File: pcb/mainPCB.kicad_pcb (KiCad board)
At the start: 4 copper layers, 147.3 x 73 mm, 74 parts, among them J1 Inputs, J10 Conn_01x02_Male, J11 Conn_01x04_Male, J12 Conn_01x04_Male, J13 Conn_01x04_Male, J2 ESP32_left, J3 ESP32_right, J4 F9P_left_top, J5 F9P left bottom, J6 F9P right, J7 Motor A, J8 Motor B, J9 Power, K1 G5LE-1, U1 MMA8452Q, U2 AZ1117-5.0, U3 AZ1117-3.3, U4 AZ1117-5.0, U5 VNH7070AS, U6 VNH7070AS, U7 ADS1115IDGS, U8 PCA9306DCTR

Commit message: first version of the new feature set
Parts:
- removed J2: ESP32_left, Connector_PinSocket_2.54mm:PinSocket_1x15_P2.54mm_Vertical
- removed J6: F9P right, Connector_PinSocket_2.54mm:PinSocket_1x08_P2.54mm_Vertical
- added C23: 100p, Capacitor_SMD:C_0805_2012Metric, F.Cu at (133.8, 82.1)
- added C24: 1n, Capacitor_SMD:C_0805_2012Metric, F.Cu at (130.4, 74.1)
- added C25: 22u, Capacitor_SMD:C_0805_2012Metric, F.Cu at (130.2, 51.6)
- added C26: 100n, Capacitor_SMD:C_0805_2012Metric, F.Cu at (128.1, 51.6)
- added C27: 100n, Capacitor_SMD:C_0805_2012Metric, F.Cu at (118.2, 52.4)
- added C28: 100n, Capacitor_SMD:C_0805_2012Metric, F.Cu at (170.1, 55.4)
- added C29: 100n, Capacitor_SMD:C_0805_2012Metric, F.Cu at (159.8, 60.4)
- added C30: 100n, Capacitor_SMD:C_0805_2012Metric, F.Cu at (159.8, 62.5)
- added C31: 2.2u, Capacitor_SMD:C_0805_2012Metric, F.Cu at (159.8, 64.6)
- added C32: 100n, Capacitor_SMD:C_0805_2012Metric, F.Cu at (33.9, 90.6)
- added C33: 560u, Capacitor_SMD:CP_Elec_10x10.5, F.Cu at (44.1, 87.5)
- added C34: 1n/2000V, Capacitor_SMD:C_1206_3216Metric, F.Cu at (91.7, 51.7)
- added C35: 100n/16V, Capacitor_SMD:C_0805_2012Metric, F.Cu at (114.0, 54.0)
- added C36: 100n, Capacitor_SMD:C_0805_2012Metric, F.Cu at (97.8, 68.7)
- added C37: 22u, Capacitor_SMD:C_0805_2012Metric, F.Cu at (109.6, 67.3)
- added C38: 100n, Capacitor_SMD:C_0805_2012Metric, F.Cu at (109.6, 69.5)
- added C39: 100n, Capacitor_SMD:C_0805_2012Metric, F.Cu at (97.9, 72.1)
- added C40: 2.2u, Capacitor_SMD:C_0805_2012Metric, F.Cu at (97.9, 74.3)
- added C41: 100n, Capacitor_SMD:C_0805_2012Metric, F.Cu at (103.6, 74.6)
- added C42: 100n, Capacitor_SMD:C_0805_2012Metric, F.Cu at (151.1, 92.4)
- added C43: 100n, Capacitor_SMD:C_0805_2012Metric, F.Cu at (153.4, 89.5)
- added C44: 100n, Capacitor_SMD:C_0805_2012Metric, F.Cu at (156.9, 89.5)
- added C45: 100n, Capacitor_SMD:C_0805_2012Metric, F.Cu at (159.4, 92.4)
- added C46: 100n, Capacitor_SMD:C_0805_2012Metric, F.Cu at (156.4, 100.3)
- added C47: 10n, Capacitor_SMD:C_0805_2012Metric, F.Cu at (175.4, 94.4)
- added C48: 100n, Capacitor_SMD:C_0805_2012Metric, F.Cu at (173.2, 94.4)
- added C49: 100n, Capacitor_SMD:C_0805_2012Metric, F.Cu at (169.4, 97.7)
- added C50: 10u, Capacitor_SMD:C_0805_2012Metric, F.Cu at (169.4, 93.4)
- added C51: 100n, Capacitor_SMD:C_0805_2012Metric, F.Cu at (169.4, 95.6)
- added D10: BAT54C, Package_TO_SOT_SMD:SOT-23, F.Cu at (149.2, 79.0)
- added D11: SD0805S020S1R0, Diode_SMD:D_0805_2012Metric, F.Cu at (161.2, 54.4)
- added D4: LED/red, Capacitor_SMD:C_0805_2012Metric, F.Cu at (75.8, 106.7)
- added D5: LED/red, Capacitor_SMD:C_0805_2012Metric, F.Cu at (63.8, 48.5)
- added D6: LED/red, Capacitor_SMD:C_0805_2012Metric, F.Cu at (68.1, 48.5)
- added D7: SD0805S020S1R0, Diode_SMD:D_0805_2012Metric, F.Cu at (67.6, 55.4)
- added D8: SD0805S020S1R0, Diode_SMD:D_0805_2012Metric, F.Cu at (53.8, 94.7)
- added D9: LED/green, Capacitor_SMD:C_0805_2012Metric, F.Cu at (79.2, 106.8)
- added F1: 12A/slow, ICs_own:Fuse_1206_3216Metric, F.Cu at (53.1, 53.2)
- added FB1: 600R/2A, Inductor_SMD:L_0805_2012Metric, F.Cu at (109.6, 71.6)
- added H6: MountingHole, MountingHole:MountingHole_3.2mm_M3_DIN965, F.Cu at (28.6, 65.5)
- added H7: MountingHole, MountingHole:MountingHole_3.2mm_M3_DIN965, F.Cu at (28.6, 82.4)
- added H8: MountingHole, MountingHole:MountingHole_3.2mm_M3_DIN965, F.Cu at (115.2, 59.1)
- added IC1: FXL6408UMX, ICs_own:QFN40P180X260X55-16N, F.Cu at (73.5, 97.9)
- added IC2: ATA6561-GAQW-N, ICs_own:SOIC127P600X175-8N, F.Cu at (123.1, 51.5)
- added IC3: ICL3221EIVZ, ICs_own:SOP65P640X120-16N, F.Cu at (155.3, 95.1)
- added J14: USB_B_Micro, Connector_own:USB_Micro-B_Molex-105017-0001, F.Cu at (174.6, 52.8)
- added J15: RJ45_Amphenol_RJMG1BD3B8K1ANR, Connector_own:RJ45_Amphenol_RJMG1BD3B8K1ANR, F.Cu at (106.9, 54.9)
- added J16: DB9_Male_MountingHoles, Connector_own:LD09P33E4GV00LF, F.Cu at (179.4, 74.0)
- added J17: SM04B-SRSS-TB(LF)(SN), Connector_own:JST_SH_SM04B-SRSS-TB_1x04-1MP_P1.00mm_Horizontal, F.Cu at (156.5, 106.9)
- added J18: PTSM-Header-Horizontal-2, Connector_own:1814841, F.Cu at (116.8, 44.7)
- added K2: CP1SA-12V-Z, Relay_own:CP1SA12VZ, F.Cu at (82.0, 61.6)
- added L1: 22u, Inductor_SMD:L_0805_2012Metric, F.Cu at (132.8, 51.6)
- added PS1: V78E05-1000-SMT-TR, ICs_own:SOP254P1140X825-10N, F.Cu at (59.9, 86.6)
- added Q1: BC817-40,215, ICs_own:SOT95P230X110-3N, F.Cu at (154.4, 71.1)
- added Q2: BC817-40,215, ICs_own:SOT95P230X110-3N, F.Cu at (149.0, 71.1)
- added R23: 2.4k, Resistor_SMD:R_0805_2012Metric, F.Cu at (157.2, 49.8)
- added R24: 2.4k, Resistor_SMD:R_0805_2012Metric, F.Cu at (162.7, 49.8)
- added R25: 240, Resistor_SMD:R_0805_2012Metric, F.Cu at (139.8, 51.6)
- added R26: 2.4k, Resistor_SMD:R_0805_2012Metric, F.Cu at (139.0, 92.5)
- added R27: 2.4k, Resistor_SMD:R_0805_2012Metric, F.Cu at (139.1, 90.2)
- added R28: 220k, Resistor_SMD:R_0805_2012Metric, F.Cu at (133.7, 79.8)
- added R29: 2.4k, Resistor_SMD:R_0805_2012Metric, F.Cu at (122.7, 90.2)
- added R30: 2.4k, Resistor_SMD:R_0805_2012Metric, F.Cu at (122.7, 92.2)
- added R31: 2.4k, Resistor_SMD:R_0805_2012Metric, F.Cu at (130.5, 69.7)
- added R32: 620, Resistor_SMD:R_0805_2012Metric, F.Cu at (130.5, 71.9)
- added R33: 120, Resistor_SMD:R_0805_2012Metric, F.Cu at (119.6, 55.8)
- added R34: 22.1k, Resistor_SMD:R_0805_2012Metric, F.Cu at (165.9, 55.4)
- added R35: 47k, Resistor_SMD:R_0805_2012Metric, F.Cu at (165.9, 53.2)
- added R36: 1k, Resistor_SMD:R_0805_2012Metric, F.Cu at (160.5, 57.3)
- added R37: 1k, Resistor_SMD:R_0805_2012Metric, F.Cu at (151.8, 64.5)
- added R38: 120, Resistor_SMD:R_0805_2012Metric, F.Cu at (143.3, 58.0)
- added R39: 120, Resistor_SMD:R_0805_2012Metric, F.Cu at (141.0, 58.0)
- added R40: 1k, Resistor_SMD:R_0805_2012Metric, F.Cu at (151.8, 66.9)
- added R41: 120, Resistor_SMD:R_0805_2012Metric, F.Cu at (153.6, 79.0)
- added R42: 0, Resistor_SMD:R_0805_2012Metric, F.Cu at (91.7, 56.2)
- added R43: 2.4k, Resistor_SMD:R_0805_2012Metric, F.Cu at (91.7, 46.8)
- added R44: 0, Resistor_SMD:R_0805_2012Metric, F.Cu at (113.9, 50.8)
- added R45: 49.9, Resistor_SMD:R_0805_2012Metric, F.Cu at (107.9, 61.7)
- added R46: 49.9, Resistor_SMD:R_0805_2012Metric, F.Cu at (97.8, 64.3)
- added R47: 49.9, Resistor_SMD:R_0805_2012Metric, F.Cu at (107.8, 65.0)
- added R48: 12.1k, Resistor_SMD:R_0805_2012Metric, F.Cu at (97.7, 66.4)
- added R49: 49.9, Resistor_SMD:R_0805_2012Metric, F.Cu at (97.7, 61.1)
- added R50: 2.4k, Resistor_SMD:R_0805_2012Metric, F.Cu at (113.9, 47.5)
- added R51: 2.4k, Resistor_SMD:R_0805_2012Metric, F.Cu at (111.0, 76.6)
- added R52: 2.4k, Resistor_SMD:R_0805_2012Metric, F.Cu at (111.0, 78.9)
- added R53: 2.4k, Resistor_SMD:R_0805_2012Metric, F.Cu at (111.0, 74.5)
- added R54: 24, Resistor_SMD:R_0805_2012Metric, F.Cu at (169.4, 91.3)
- added SW1: SW_Push, Button_Switch_SMD:SW_SPST_PTS645, F.Cu at (127.0, 97.3)
- added U10: NUD3124LT1G, ICs_own:SOT95P237X100-3N, F.Cu at (72.3, 70.2)
- added U11: LAN8720A, Package_DFN_QFN:QFN-24-1EP_4x4mm_P0.5mm_EP2.6x2.6mm, F.Cu at (102.8, 70.7)
- added U12: LSM9DS1, Package_LGA:LGA-24L_3x3.5mm_P0.43mm, F.Cu at (174.3, 98.2)
- added U9: VNH7070AS, Package_SO:SOIC-16_3.9x9.9mm_P1.27mm, F.Cu at (28.4, 91.2)
- C1, C10, C21, C3, C9: footprint Capacitor_SMD:C_0805_2012Metric_Pad1.15x1.40mm_HandSolder -> Capacitor_SMD:C_0805_2012Metric
- C11: value 22n -> 22u; footprint Capacitor_SMD:C_0805_2012Metric_Pad1.15x1.40mm_HandSolder -> Capacitor_SMD:C_0805_2012Metric
- C12, C8: value 10u -> 100n; footprint Capacitor_SMD:C_0805_2012Metric_Pad1.15x1.40mm_HandSolder -> Capacitor_SMD:C_0805_2012Metric
- C13: value 100n -> 560u; footprint Capacitor_SMD:C_0805_2012Metric_Pad1.15x1.40mm_HandSolder -> Capacitor_SMD:CP_Elec_10x10.5
- C14: value 470u -> 1n; footprint Capacitor_THT:CP_Radial_D8.0mm_P3.80mm -> Capacitor_SMD:C_0805_2012Metric
- C15: value 100n -> 1n; footprint Capacitor_SMD:C_0805_2012Metric_Pad1.15x1.40mm_HandSolder -> Capacitor_SMD:C_0805_2012Metric
- C16: value 22u -> 100p; footprint Capacitor_SMD:C_0805_2012Metric_Pad1.15x1.40mm_HandSolder -> Capacitor_SMD:C_0805_2012Metric
- C17, C18: value 1n -> 100p; footprint Capacitor_SMD:C_0805_2012Metric_Pad1.15x1.40mm_HandSolder -> Capacitor_SMD:C_0805_2012Metric
- C19: value 100p -> 100n; footprint Capacitor_SMD:C_0805_2012Metric_Pad1.15x1.40mm_HandSolder -> Capacitor_SMD:C_0805_2012Metric
- C2: value 4.7u -> 100n; footprint Capacitor_SMD:C_0805_2012Metric_Pad1.15x1.40mm_HandSolder -> Capacitor_SMD:C_0805_2012Metric
- C20: value 100p -> 22u; footprint Capacitor_SMD:C_0805_2012Metric_Pad1.15x1.40mm_HandSolder -> Capacitor_SMD:C_0805_2012Metric
- C22: value 100p -> 560u; footprint Capacitor_SMD:C_0805_2012Metric_Pad1.15x1.40mm_HandSolder -> Capacitor_SMD:CP_Elec_10x10.5
- C4: value 22u -> 100n; footprint Capacitor_SMD:C_0805_2012Metric_Pad1.15x1.40mm_HandSolder -> Capacitor_SMD:C_0805_2012Metric
- C5: value 2200u -> 22u; footprint Capacitor_THT:CP_Radial_D14.0mm_P5.00mm -> Capacitor_SMD:C_0805_2012Metric
- C6: value 10u -> 560u; footprint Capacitor_SMD:C_0805_2012Metric_Pad1.15x1.40mm_HandSolder -> Capacitor_SMD:CP_Elec_10x10.5
- C7: value 22u -> 10u; footprint Capacitor_SMD:C_0805_2012Metric_Pad1.15x1.40mm_HandSolder -> Capacitor_SMD:C_0805_2012Metric
- D1: value Network -> LED/blue; footprint LED_SMD:LED_0805_2012Metric_Pad1.15x1.40mm_HandSolder -> Capacitor_SMD:C_0805_2012Metric
- D2: value NTRIP -> LED/blue; footprint LED_SMD:LED_0805_2012Metric_Pad1.15x1.40mm_HandSolder -> Capacitor_SMD:C_0805_2012Metric
- D3: value SD0805S020S1R0 -> LED/green; footprint Diode_SMD:D_0805_2012Metric_Pad1.15x1.40mm_HandSolder -> Capacitor_SMD:C_0805_2012Metric
- H5: footprint MountingHole:MountingHole_4.3mm_M4_DIN965 -> MountingHole:MountingHole_3.2mm_M3_DIN965
- J1: value Inputs -> PTSM-Header-Horizontal-6; footprint TerminalBlock_Phoenix:TerminalBlock_Phoenix_MPT-0,5-8-2.54_1x08_P2.54mm_Horizontal -> Connector_own:1814883
- J10: value Conn_01x02_Male -> Conn_01x08_Female; footprint Connector_PinHeader_2.54mm:PinHeader_1x02_P2.54mm_Vertical -> Connector_PinSocket_2.54mm:PinSocket_1x08_P2.54mm_Vertical
- J11: value Conn_01x04_Male -> Conn_01x08_Female; footprint Connector_PinHeader_2.54mm:PinHeader_1x04_P2.54mm_Vertical -> Connector_PinSocket_2.54mm:PinSocket_1x08_P2.54mm_Vertical
- J12: value Conn_01x04_Male -> Conn_02x02_Odd_Even; footprint Connector_PinHeader_2.54mm:PinHeader_1x04_P2.54mm_Vertical -> Connector_PinHeader_2.54mm:PinHeader_2x02_P2.54mm_Horizontal
- J13: value Conn_01x04_Male -> SM04B-SRSS-TB(LF)(SN); footprint Connector_PinHeader_2.54mm:PinHeader_1x04_P2.54mm_Vertical -> Connector_own:JST_SH_SM04B-SRSS-TB_1x04-1MP_P1.00mm_Horizontal
- J3: value ESP32_right -> PTSM-Header-Horizontal-7; footprint Connector_PinSocket_2.54mm:PinSocket_1x15_P2.54mm_Vertical -> Connector_own:1814896
- J4: value F9P_left_top -> CCA-Header-Horizontal-4; footprint Connector_PinSocket_2.54mm:PinSocket_1x08_P2.54mm_Vertical -> Connector_own:1836366
- J5: value F9P left bottom -> PTSM-Header-Horizontal-5; footprint Connector_PinSocket_2.54mm:PinSocket_1x08_P2.54mm_Vertical -> Connector_own:1814870
- J7: value Motor A -> Conn_01x04_Male; footprint TerminalBlock_Phoenix:TerminalBlock_Phoenix_MKDS-1,5-2-5.08_1x02_P5.08mm_Horizontal -> Connector_PinHeader_2.54mm:PinHeader_1x04_P2.54mm_Horizontal
- J8: value Motor B -> Conn_01x04_Male; footprint TerminalBlock_Phoenix:TerminalBlock_Phoenix_MKDS-1,5-2-5.08_1x02_P5.08mm_Horizontal -> Connector_PinHeader_2.54mm:PinHeader_1x04_P2.54mm_Vertical
- J9: value Power -> Conn_01x08_Female; footprint TerminalBlock_Phoenix:TerminalBlock_Phoenix_MKDS-1,5-2-5.08_1x02_P5.08mm_Horizontal -> Connector_PinSocket_2.54mm:PinSocket_1x08_P2.54mm_Vertical
- K1: value G5LE-1 -> CP1SA-12V-Z; footprint Relay_THT:Relay_SPDT_Omron-G5LE-1 -> Relay_own:CP1SA12VZ
- R1: value 47 -> 120; footprint Resistor_SMD:R_0805_2012Metric_Pad1.15x1.40mm_HandSolder -> Resistor_SMD:R_0805_2012Metric
- R10: value 1k -> 47k; footprint Resistor_SMD:R_0805_2012Metric_Pad1.15x1.40mm_HandSolder -> Resistor_SMD:R_0805_2012Metric
- R11, R12, R18, R20, R7, R8, R9: footprint Resistor_SMD:R_0805_2012Metric_Pad1.15x1.40mm_HandSolder -> Resistor_SMD:R_0805_2012Metric
- R13: value 2.4k -> 1k; footprint Resistor_SMD:R_0805_2012Metric_Pad1.15x1.40mm_HandSolder -> Resistor_SMD:R_0805_2012Metric
- R14: value 620 -> 2.4k; footprint Resistor_SMD:R_0805_2012Metric_Pad1.15x1.40mm_HandSolder -> Resistor_SMD:R_0805_2012Metric
- R15: value 2.4k -> 24; footprint Resistor_SMD:R_0805_2012Metric_Pad1.15x1.40mm_HandSolder -> Resistor_SMD:R_0805_2012Metric
- R16: value 620 -> 24; footprint Resistor_SMD:R_0805_2012Metric_Pad1.15x1.40mm_HandSolder -> Resistor_SMD:R_0805_2012Metric
- R17, R21: value 2.4k -> 620; footprint Resistor_SMD:R_0805_2012Metric_Pad1.15x1.40mm_HandSolder -> Resistor_SMD:R_0805_2012Metric
- R19: value 220k -> 620; footprint Resistor_SMD:R_0805_2012Metric_Pad1.15x1.40mm_HandSolder -> Resistor_SMD:R_0805_2012Metric
- R2, R3: value 160 -> 620; footprint Resistor_SMD:R_0805_2012Metric_Pad1.15x1.40mm_HandSolder -> Resistor_SMD:R_0805_2012Metric
- R22: value 24 -> 2.4k; footprint Resistor_SMD:R_0805_2012Metric_Pad1.15x1.40mm_HandSolder -> Resistor_SMD:R_0805_2012Metric
- R4, R5: value 4.7k -> 620; footprint Resistor_SMD:R_0805_2012Metric_Pad1.15x1.40mm_HandSolder -> Resistor_SMD:R_0805_2012Metric
- R6: value 24 -> 47k; footprint Resistor_SMD:R_0805_2012Metric_Pad1.15x1.40mm_HandSolder -> Resistor_SMD:R_0805_2012Metric
- U1: value MMA8452Q -> ESP32-WROOM-32; footprint Package_LGA:LGA-16_3x3mm_P0.5mm_LayoutBorder3x5y -> RF_Module:ESP32-WROOM-32
- U2: value AZ1117-5.0 -> AZ1117-3.3
- U3: value AZ1117-3.3 -> VNH7070AS; footprint Package_TO_SOT_SMD:SOT-223-3_TabPin2 -> Package_SO:SOIC-16_3.9x9.9mm_P1.27mm
- U4: value AZ1117-5.0 -> ADS1115IDGS; footprint Package_TO_SOT_SMD:SOT-223-3_TabPin2 -> Package_SO:MSOP-10_3x3mm_P0.5mm
- U6: value VNH7070AS -> PCA9306DCTR; footprint Package_SO:SOIC-16_3.9x9.9mm_P1.27mm -> Package_SO:SSOP-8_2.95x2.8mm_P0.65mm
- U7: value ADS1115IDGS -> TPD3E001DRLR; footprint Package_SO:MSOP-10_3x3mm_P0.5mm -> Package_TO_SOT_SMD:SOT-553
- U8: value PCA9306DCTR -> CP2102N-A01-GQFN24; footprint Package_SO:SSOP-8_2.95x2.8mm_P0.65mm -> Package_DFN_QFN:QFN-24-1EP_4x4mm_P0.5mm_EP2.6x2.6mm
- moved U5 237.4 mm to (28.4, 73.9), turned to 0 degrees
- moved C13 219.7 mm to (44.1, 59.2), turned to 270 degrees
- moved K1 216.7 mm to (58.9, 66.3), turned to 90 degrees
- moved C12 215.3 mm to (33.7, 55.8)
- moved D3 213.6 mm to (72.6, 106.7)
- moved R6 211.7 mm to (77.9, 97.2), turned to 270 degrees
- moved U3 190.7 mm to (28.3, 56.8), turned to 0 degrees
- moved R7 190.4 mm to (58.0, 108.5), turned to 0 degrees
- moved R12 190.2 mm to (58.0, 97.7), turned to 0 degrees
- moved R11 189.8 mm to (58.0, 99.8), turned to 0 degrees
- moved C8 189.4 mm to (59.1, 79.2), turned to 0 degrees
- moved R8 188.4 mm to (58.0, 106.3), turned to 0 degrees
- moved D2 188.3 mm to (69.3, 106.7), turned to 90 degrees
- moved R9 187.0 mm to (58.0, 104.1), turned to 0 degrees
- moved J8 185.0 mm to (76.5, 82.7)
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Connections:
- C1 pad 1: +3V3 -> GND
- C1 pad 2: GND -> Net-(C1-Pad2)
- C10 pad 1: Net-(C10-Pad1) -> +5V
- C11 pad 1: GND -> +3V3
- C11 pad 2: Net-(C11-Pad2) -> GND
- C14 pad 1: +12V -> /Input_1/output
- C15 pad 1: +12V -> /Input_2/output
- C16 pad 1: +5V -> Net-(C16-Pad1)
- C17 pad 1: /Workswitch/output -> Net-(C17-Pad1)
- C18 pad 1: /AutosteerSwitch/output -> Net-(C18-Pad1)
- C20 pad 1: Net-(C20-Pad1) -> Net-(C19-Pad1)
- C21 pad 1: +5V -> +12V
- C22 pad 1: Net-(C22-Pad1) -> +12V
- C3 pad 1: Net-(C3-Pad1) -> /ESP_EN
- C4 pad 1: GND -> +3V3
- C4 pad 2: +3V3 -> GND
- C5 pad 1: +12V -> +3V3
- C6 pad 1: +5V -> Net-(C6-Pad1)
- C7 pad 1: +3V3 -> Net-(C6-Pad1)
- C8 pad 1: +12V -> Net-(C8-Pad1)
- D3 pad 1: +12V -> GND
- J1 pad 1: /Workswitch/input -> Net-(C1-Pad2)
- J1 pad 2: Net-(C11-Pad2) -> /Input_1/input
- J1 pad 3: /AutosteerSwitch/input -> Net-(C1-Pad2)
- J1 pad 4: Net-(C11-Pad2) -> /Input_2/input
- J1 pad 5: Net-(J1-Pad5) -> Net-(C1-Pad2)
- J1 pad 6: /SteeringAngle/In_A -> /Input_3/input
- J10 pad 1: +5V -> /F9P/RX2
- J10 pad 2: /SteeringAngle/In_A -> Net-(J10-Pad2)
- J11 pad 1: /I2C_SDA -> Net-(J11-Pad1)
- J11 pad 2: /I2C_SCL -> GND
- J11 pad 4: +3V3 -> +5V
- J12 pad 1: +12V -> Net-(IC2-Pad1)
- J12 pad 2: +5V -> /CAN_TXD
- J12 pad 3: +3V3 -> Net-(IC2-Pad6)
- J12 pad 4: GND -> Net-(J12-Pad4)
- J13 pad 1: Net-(J13-Pad1) -> GND
- J13 pad 2: Net-(J13-Pad2) -> +3V3
- J13 pad 3: GND -> /I2C_3_SCL
- J13 pad 4: +5V -> /I2C_3_SDA
- J3 pad 1: /VSPI_MOSI -> /Relais/COM
- J3 pad 2: /I2C_SCL -> /Relais/NC
- J3 pad 3: Net-(J3-Pad3) -> /Relais/NO
- J3 pad 4: Net-(J3-Pad4) -> /sheet5C9DA53F/outB
- J3 pad 5: /I2C_SDA -> GND
- J3 pad 6: /VSPI_MISO -> /sheet5C9DA53F/outA
- J3 pad 7: /VSPI_CLK -> GND
- J4 pad 1: Net-(J4-Pad1) -> GND
- J4 pad 2: Net-(J4-Pad2) -> /powerSupply/V_In_12V
- J4 pad 3: Net-(J3-Pad9) -> /motorDriverA/outA
- J4 pad 4: Net-(J4-Pad4) -> /motorDriverA/outB
- J5 pad 1: Net-(J3-Pad10) -> Net-(J5-Pad1)
- J5 pad 3: Net-(J5-Pad3) -> GND
- J7 pad 1: /motorDriverA/outA -> +5V
- J7 pad 2: /motorDriverA/outB -> GND
- J8 pad 1: /motorDriverB/outA -> +3V3
- J8 pad 2: /motorDriverB/outB -> GND
- J9 pad 1: /powerSupply/V_In_12V -> /RXD01
- J9 pad 2: GND -> /TXD01
- K1 pad 2: +12V -> Net-(D5-Pad1)
- K1 pad 3: /powerSupply/V_In_12V -> +12V
- K1 pad 4: Net-(K1-Pad4) -> GND
- K1 pad 5: GND -> Net-(D6-Pad2)
- R1 pad 2: Net-(C11-Pad2) -> Net-(C1-Pad2)
- R10 pad 1: Net-(R10-Pad1) -> +3V3
- R10 pad 2: /motorDriverB/INA -> /ESP_EN
- R11 pad 1: Net-(R11-Pad1) -> /motorDriverA/INA
- R11 pad 2: /motorDriverB/InB -> /M1_INA
- R12 pad 1: Net-(R12-Pad1) -> /motorDriverA/InB
- R12 pad 2: /motorDriverB/PWM -> /M1_INB
- R13 pad 1: /Workswitch/output -> /motorDriverA/PWM
- R13 pad 2: /Workswitch/input -> /M1_PWM
- R14 pad 1: /Workswitch/output -> GND
- R14 pad 2: GND -> Net-(D5-Pad2)
- R15 pad 1: /AutosteerSwitch/output -> Net-(D7-Pad2)
- R15 pad 2: /AutosteerSwitch/input -> Net-(D5-Pad1)
- R16 pad 1: /AutosteerSwitch/output -> Net-(D7-Pad2)
- R16 pad 2: GND -> Net-(D5-Pad1)
- R17 pad 1: Net-(C19-Pad1) -> +3V3
- R17 pad 2: /SteeringAngle/IN_B -> Net-(D9-Pad2)
- R18 pad 1: Net-(C20-Pad1) -> /Input_1/output
- R18 pad 2: /SteeringAngle/In_A -> /Input_1/input
- R19 pad 1: +5V -> /Input_1/output
- R19 pad 2: Net-(C22-Pad1) -> GND
- R2 pad 1: Net-(J2-Pad6) -> Net-(D1-Pad2)
- R2 pad 2: Net-(D1-Pad2) -> Net-(IC1-Pad7)
- R20 pad 1: Net-(J13-Pad2) -> /Input_2/output
- R20 pad 2: +5V -> /Input_2/input
- R21 pad 1: Net-(J13-Pad1) -> /Input_2/output
- R21 pad 2: +5V -> GND
- R22 pad 1: Net-(D3-Pad2) -> Net-(C16-Pad1)
- R22 pad 2: /powerSupply/V_In_12V -> Net-(J5-Pad5)
- R3 pad 1: Net-(J2-Pad7) -> Net-(D2-Pad2)
- R3 pad 2: Net-(D2-Pad2) -> Net-(IC1-Pad8)
- R4 pad 1: +3V3 -> Net-(D3-Pad2)
- R4 pad 2: /I2C_SCL -> Net-(IC1-Pad11)
- R5 pad 1: +3V3 -> Net-(D4-Pad2)
- R5 pad 2: /I2C_SDA -> Net-(IC1-Pad12)
- R6 pad 1: Net-(D3-Pad2) -> +3V3
- R6 pad 2: /powerSupply/V_In_12V -> Net-(IC1-Pad10)
- R7 pad 1: Net-(R7-Pad1) -> /sheet5C9DA53F/INA
- R7 pad 2: /motorDriverA/INA -> /M2_INA
- R8 pad 1: Net-(R8-Pad1) -> /sheet5C9DA53F/InB
- R8 pad 2: /motorDriverA/InB -> /M2_INB
- R9 pad 1: Net-(R9-Pad1) -> /sheet5C9DA53F/PWM
- R9 pad 2: /motorDriverA/PWM -> /M2_PWM
- U1 pad 1: +3V3 -> GND
- U1 pad 10: GND -> /LAN8720/EMAC_RXD0:GPIO25
- U1 pad 11: Net-(U1-Pad11) -> /LAN8720/EMAC_RXD1:GPIO26
- U1 pad 12: GND -> /LAN8720/EMAC_RX_CRS_DV:GPIO27
- U1 pad 13: (no net) -> /RXD01
- U1 pad 14: +3V3 -> /M2_PWM
- U1 pad 15: (no net) -> GND
- U1 pad 16: (no net) -> /TXD01
- U1 pad 2: Net-(C3-Pad1) -> +3V3
- U1 pad 3: (no net) -> /ESP_EN
- U1 pad 4: /I2C_SCL -> /Input_1/output
- U1 pad 5: GND -> /Input_2/output
- U1 pad 6: /I2C_SDA -> /Input_3/output
- U1 pad 7: GND -> /CAN_RXD
- U1 pad 8: (no net) -> /I2C_3_SDA
- U1 pad 9: Net-(U1-Pad9) -> /I2C_3_SCL
- U2 pad 2: +5V -> +3V3
- U2 pad 3: +12V -> +5V
- U3 pad 2: +3V3 -> /motorDriverA/outA
- U3 pad 3: +5V -> /motorDriverA/INA
- U4 pad 2: +5V -> Net-(U4-Pad2)
- U4 pad 3: +12V -> GND
- U5 pad 11: Net-(R9-Pad1) -> /motorDriverA/PWM
- U5 pad 3: Net-(R7-Pad1) -> /motorDriverA/INA
- U5 pad 6: Net-(R8-Pad1) -> /motorDriverA/InB
- U6 pad 2: /motorDriverB/outA -> +3V3
- U6 pad 3: Net-(R10-Pad1) -> /I2C_3_SDA
- U6 pad 4: +12V -> /I2C_3_SCL
- U6 pad 5: +12V -> /I2C_5_SCL
- U6 pad 6: Net-(R11-Pad1) -> /I2C_5_SDA
- U6 pad 7: /motorDriverB/outB -> Net-(C23-Pad1)
- U6 pad 8: GND -> Net-(C23-Pad1)
- U7 pad 1: +5V -> Net-(J14-Pad4)
- U7 pad 2: Net-(U7-Pad2) -> Net-(J14-Pad3)
- U7 pad 4: Net-(C20-Pad1) -> Net-(J14-Pad2)
- U7 pad 5: Net-(C19-Pad1) -> Net-(C28-Pad1)
- U8 pad 1: GND -> Net-(U8-Pad1)
- U8 pad 2: +3V3 -> GND
- U8 pad 3: /I2C_SCL -> Net-(J14-Pad3)
- U8 pad 4: /I2C_SDA -> Net-(J14-Pad2)
- U8 pad 5: Net-(J13-Pad1) -> +3V3
- U8 pad 6: Net-(J13-Pad2) -> +3V3
- U8 pad 7: Net-(C22-Pad1) -> +3V3
- U8 pad 8: Net-(C22-Pad1) -> Net-(R34-Pad1)
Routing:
- net +12V: track 368.7 -> 114.4 mm, vias 30 -> 42
- net /I2C_3_SCL: track 0.00 -> 180.1 mm, vias 0 -> 8
- net /I2C_3_SDA: track 0.00 -> 177.0 mm, vias 0 -> 8
- net /sheet5C9DA53F/outB: track 0.00 -> 134.1 mm, vias 0 -> 7
- net /I2C_SCL: track 123.2 -> 0.00 mm, vias 3 -> 0
- net /usbUart/RX: track 0.00 -> 117.2 mm, vias 0 -> 4
- net /usbUart/TX: track 0.00 -> 113.6 mm, vias 0 -> 4
- net /sheet5C9DA53F/outA: track 0.00 -> 111.5 mm, vias 0 -> 5
- net /I2C_SDA: track 110.7 -> 0.00 mm, vias 2 -> 0
- net /M1_INA: track 0.00 -> 108.7 mm, vias 0 -> 4
- net /M1_INB: track 0.00 -> 103.7 mm, vias 0 -> 4
- net /RXD02: track 0.00 -> 84.6 mm, vias 0 -> 2
- net /CAN_TXD: track 0.00 -> 82.3 mm, vias 0 -> 3
- net /ESP_EN: track 0.00 -> 78.3 mm, vias 0 -> 2
- net /Input_1/output: track 0.00 -> 75.5 mm, vias 0 -> 2
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- added copper zone on B.Cu, net /powerSupply/V_In_12V
- added copper zone on F.Cu, net /powerSupply/V_In_12V
- added copper zone on F.Cu, net Net-(D5-Pad1)
- removed copper zone on B.Cu, net +12V
- removed copper zone on B.Cu, net +3V3
- removed copper zone on B.Cu, net +5V
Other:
- board size 147.3 x 73 mm -> 160 x 73.2 mm
- board text added: "A0"
- board text added: "A1"
- board text added: "A2"
- board text added: "CAN"
- board text added: "CAN TX enable →"
- board text added: "CAN termination →"
- board text added: "COM"
- board text added: "ESP-F9P-IO-Board Version 2.0"
- board text added: "Error"
- board text added: "H"
- board text added: "I1"
- board text added: "I2"
- board text added: "I3"
- board text added: "L"
- board text added: "M1A"
- board text added: "M1B"
- board text added: "M2A"
- board text added: "M2B"
- board text added: "NC"
- board text added: "NO"
- board text added: "Setup"
- board text added: "polarity"
- board text added: "qwiic"
- board text added: "relay"
- board text added: "↑Error"
- board text added: "↑Power"
- board text added: "↑Status"
- board text added: "↓Navigation"
- board text added: "↓Network"
- board text removed: "- +"
- board text removed: "3,3V"
- board text removed: "5V on S1"
- board text removed: "A1 A2"
- board text removed: "AS +"
- board text removed: "B1 B2"
- board text removed: "EN"
- board text removed: "ESP32 Antenna"
- board text removed: "F9P - GND"
- board text removed: "F9P - RX2"
- board text removed: "F9P - TX2"
- board text removed: "NTRIP"
- board text removed: "Network"
- board text removed: "S1 S2 SG"
- board text removed: "WS +"
- board text removed: "x"
- board text removed: "y"

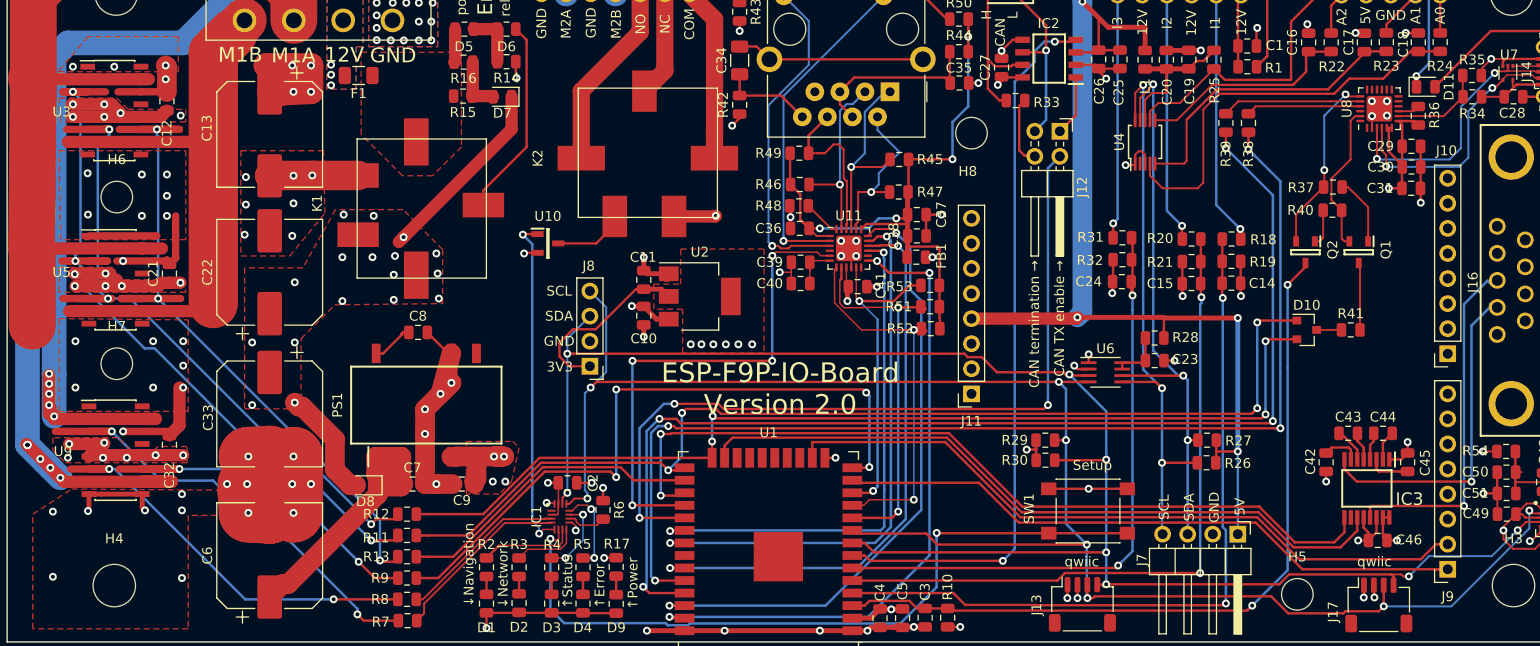
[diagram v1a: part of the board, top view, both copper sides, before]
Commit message: Added labels, added coper on the back to balance (avoid bending)
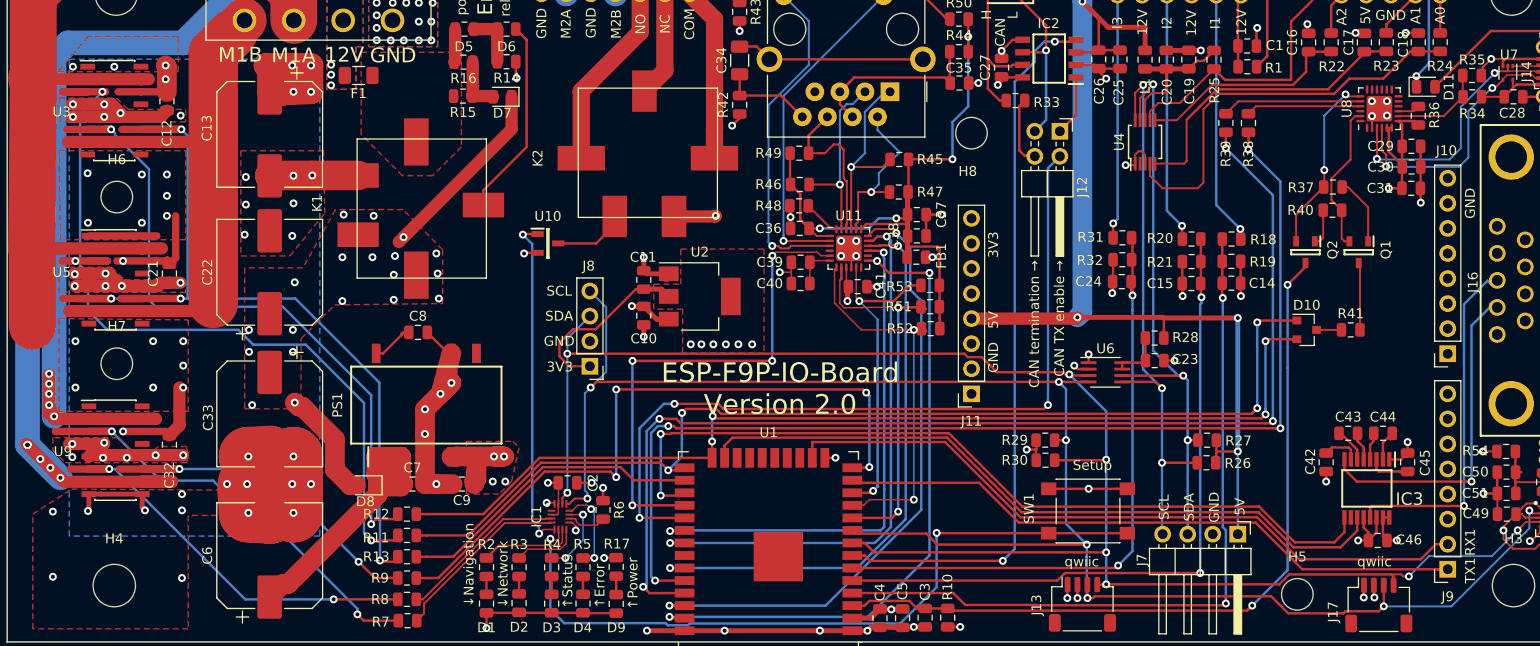
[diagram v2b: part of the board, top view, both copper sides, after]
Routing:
- net /motorDriverA/INA: track 77.5 -> 86.6 mm
- net /motorDriverA/InB: track 72.4 -> 80.5 mm
- net /motorDriverA/PWM: track 73.1 -> 79.2 mm
- net +12V: vias 42 -> 44
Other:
- board text added: "RX1"
- board text added: "TX1"

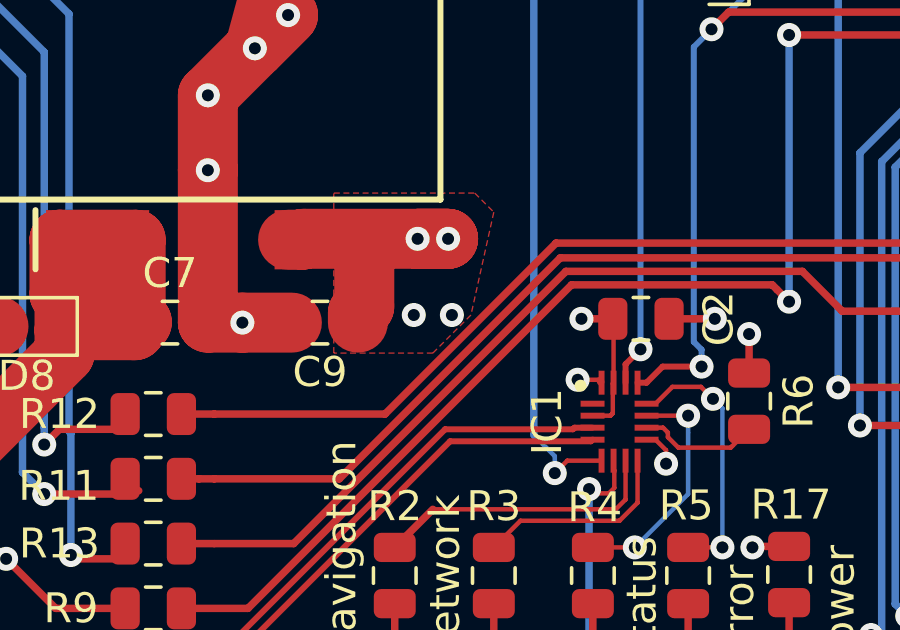
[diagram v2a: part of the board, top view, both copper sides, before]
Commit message: Updated drill files with gerber - some missmatch had happend
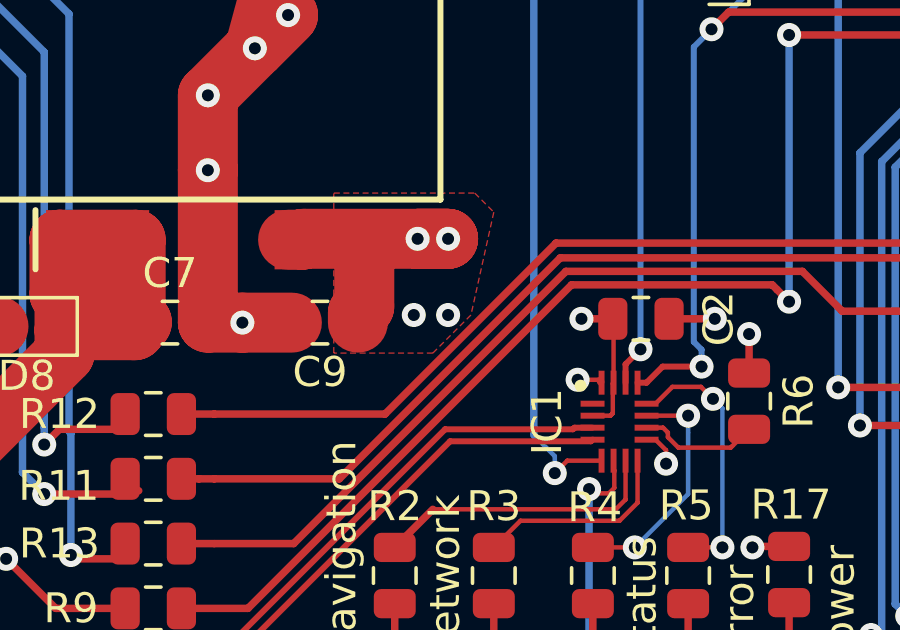
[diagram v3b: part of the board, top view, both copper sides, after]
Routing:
- net GND: vias 117 -> 115
- net +5V: vias 10 -> 12
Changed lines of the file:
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@@
   (segment (start 104.648 109.474) (end 99.822 109.474) (width 0.5) (layer F.Cu) (net 1))
   (via (at 104.648 109.474) (size 0.8) (drill 0.4) (layers F.Cu B.Cu) (net 1))
-  (via (at 67.945 94.361) (size 0.8) (drill 0.4) (layers F.Cu B.Cu) (net 1))
-  (via (at 66.675 94.361) (size 0.8) (drill 0.4) (layers F.Cu B.Cu) (net 1))
+  (via (at 67.818 94.361) (size 0.8) (drill 0.4) (layers F.Cu B.Cu) (net 9))
+  (via (at 66.675 94.361) (size 0.8) (drill 0.4) (layers F.Cu B.Cu) (net 9))
   (segment (start 75.819 107.666) (end 66.04 107.666) (width 0.25) (layer F.Cu) (net 1))
   (segment (start 66.04 107.666) (end 66.04 109.22) (width 0.25) (layer F.Cu) (net 1))

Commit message: Changed some values - RC for the inputs to lower frequencys, reduced lines on the BOM by some minor value changes
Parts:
- C16, C17, C18, C23: value 100p -> 1n
- R18, R20, R22, R23, R24, R31: value 2.4k -> 47k
- R19, R21, R32: value 620 -> 12.1k
- R25: value 240 -> 120
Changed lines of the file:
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@@
       (effects (font (size 1 1) (thickness 0.15)))
     )
-    (fp_text value 100p (at 0 1.65 90) (layer F.Fab)
+    (fp_text value 1n (at 0 1.65 90) (layer F.Fab)
       (effects (font (size 1 1) (thickness 0.15)))
     )
@@
       (effects (font (size 1 1) (thickness 0.15)))
     )
-    (fp_text value 100p (at 0 1.65 90) (layer F.Fab)
+    (fp_text value 1n (at 0 1.65 90) (layer F.Fab)
       (effects (font (size 1 1) (thickness 0.15)))
     )
@@
       (effects (font (size 1 1) (thickness 0.15)))
     )
-    (fp_text value 100p (at 0 1.65 90) (layer F.Fab)
+    (fp_text value 1n (at 0 1.65 90) (layer F.Fab)
       (effects (font (size 1 1) (thickness 0.15)))
     )
@@
       (effects (font (size 1 1) (thickness 0.15)))
     )
-    (fp_text value 100p (at 0 1.65) (layer F.Fab)
+    (fp_text value 1n (at 0 1.65) (layer F.Fab)
       (effects (font (size 1 1) (thickness 0.15)))
     )
@@
       (effects (font (size 1 1) (thickness 0.15)))
     )
-    (fp_text value 620 (at 0 1.65 180) (layer F.Fab)
+    (fp_text value 12.1k (at 0 1.65 180) (layer F.Fab)
       (effects (font (size 1 1) (thickness 0.15)))
     )
@@
       (effects (font (size 1 1) (thickness 0.15)))
     )
-    (fp_text value 2.4k (at 0 1.65 90) (layer F.Fab)
+    (fp_text value 47k (at 0 1.65 90) (layer F.Fab)
       (effects (font (size 1 1) (thickness 0.15)))
     )
@@
       (effects (font (size 1 1) (thickness 0.15)))
     )
-    (fp_text value 2.4k (at 0 1.65 90) (layer F.Fab)
+    (fp_text value 47k (at 0 1.65 90) (layer F.Fab)
       (effects (font (size 1 1) (thickness 0.15)))
     )
@@
       (effects (font (size 1 1) (thickness 0.15)))
     )
-    (fp_text value 2.4k (at 0 1.65 90) (layer F.Fab)
+    (fp_text value 47k (at 0 1.65 90) (layer F.Fab)
       (effects (font (size 1 1) (thickness 0.15)))
     )
@@
       (effects (font (size 1 1) (thickness 0.15)))
     )
-    (fp_text value 620 (at 0 1.65) (layer F.Fab)
+    (fp_text value 12.1k (at 0 1.65) (layer F.Fab)
       (effects (font (size 1 1) (thickness 0.15)))
     )
@@
       (effects (font (size 1 1) (thickness 0.15)))
     )
-    (fp_text value 2.4k (at 0 1.65 180) (layer F.Fab)
+    (fp_text value 47k (at 0 1.65 180) (layer F.Fab)
       (effects (font (size 1 1) (thickness 0.15)))
     )
@@
       (effects (font (size 1 1) (thickness 0.15)))
     )
-    (fp_text value 2.4k (at 0 1.65) (layer F.Fab)
+    (fp_text value 47k (at 0 1.65) (layer F.Fab)
       (effects (font (size 1 1) (thickness 0.15)))
     )
@@
       (effects (font (size 1 1) (thickness 0.15)))
     )
-    (fp_text value 2.4k (at 0 1.65 180) (layer F.Fab)
+    (fp_text value 47k (at 0 1.65 180) (layer F.Fab)
       (effects (font (size 1 1) (thickness 0.15)))
     )
@@
       (effects (font (size 1 1) (thickness 0.15)))
     )
-    (fp_text value 620 (at 0 1.65 180) (layer F.Fab)
+    (fp_text value 12.1k (at 0 1.65 180) (layer F.Fab)
       (effects (font (size 1 1) (thickness 0.15)))
     )
@@
       (effects (font (size 1 1) (thickness 0.15)))
     )
-    (fp_text value 240 (at 0 1.65 270) (layer F.Fab)
+    (fp_text value 120 (at 0 1.65 270) (layer F.Fab)
       (effects (font (size 1 1) (thickness 0.15)))
     )
@@
   (segment (start 104.648 109.474) (end 99.822 109.474) (width 0.5) (layer F.Cu) (net 1))
   (via (at 104.648 109.474) (size 0.8) (drill 0.4) (layers F.Cu B.Cu) (net 1))
-  (via (at 67.818 94.361) (size 0.8) (drill 0.4) (layers F.Cu B.Cu) (net 9))
-  (via (at 66.675 94.361) (size 0.8) (drill 0.4) (layers F.Cu B.Cu) (net 9))
   (segment (start 75.819 107.666) (end 66.04 107.666) (width 0.25) (layer F.Cu) (net 1))
   (segment (start 66.04 107.666) (end 66.04 109.22) (width 0.25) (layer F.Cu) (net 1))
@@
   (segment (start 66.04 103.983) (end 66.04 105.791) (width 0.25) (layer F.Cu) (net 7))
   (segment (start 69.342 103.983) (end 69.342 105.7425) (width 0.25) (layer F.Cu) (net 8))
+  (via (at 67.818 94.361) (size 0.8) (drill 0.4) (layers F.Cu B.Cu) (net 9))
+  (via (at 66.675 94.361) (size 0.8) (drill 0.4) (layers F.Cu B.Cu) (net 9))
   (segment (start 62.959283 91.852) (end 62.990283 91.821) (width 2) (layer F.Cu) (net 9))
   (segment (start 62.484 91.852) (end 62.959283 91.852) (width 2) (layer F.Cu) (net 9))

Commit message: Small optimization for soldermask
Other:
- rule pad_to_mask_clearance: 0.051 -> 0.03
- rule solder_mask_min_width: 0.25 -> 0.127
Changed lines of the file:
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@@
     (pad_size 1.5 0.6)
     (pad_drill 0)
-    (pad_to_mask_clearance 0.051)
-    (solder_mask_min_width 0.25)
+    (pad_to_mask_clearance 0.03)
+    (solder_mask_min_width 0.127)
+    (pad_to_paste_clearance -0.01)
     (aux_axis_origin 146.685 27.305)
     (grid_origin 165.1 38.1)

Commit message: Small optimization for soldermask
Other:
- rule pad_to_mask_clearance: 0.03 -> 0.035
- rule solder_mask_min_width: 0.127 -> 0.12
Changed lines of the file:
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@@
     (pad_size 1.5 0.6)
     (pad_drill 0)
-    (pad_to_mask_clearance 0.03)
-    (solder_mask_min_width 0.127)
+    (pad_to_mask_clearance 0.035)
+    (solder_mask_min_width 0.12)
     (pad_to_paste_clearance -0.01)
     (aux_axis_origin 146.685 27.305)
